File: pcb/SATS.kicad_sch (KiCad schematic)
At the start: 13 parts, among them J1 Raspberry_Pi_2_3, SW1 SW_Reed, SW2 SW_Reed, SW3 SW_Reed, U1 MCP23017_SP, U2 MCP23017_SP, U3 CD40109BE, U4 IRLZ14PBF

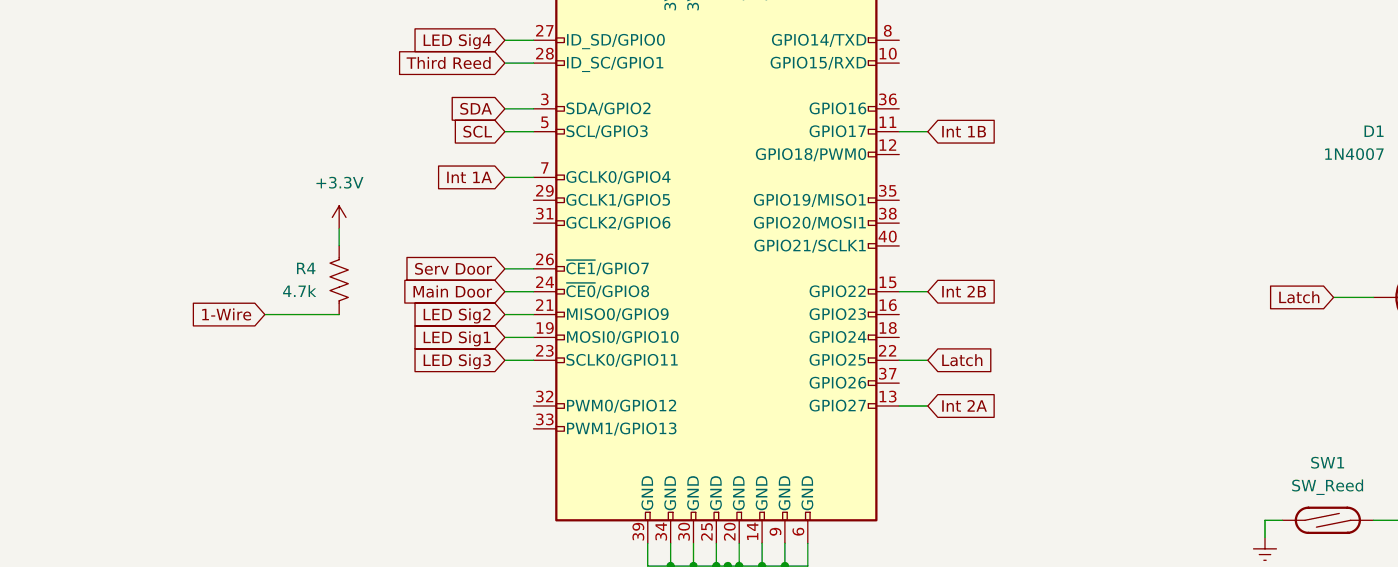
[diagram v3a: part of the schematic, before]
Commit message: actually move 1-wire
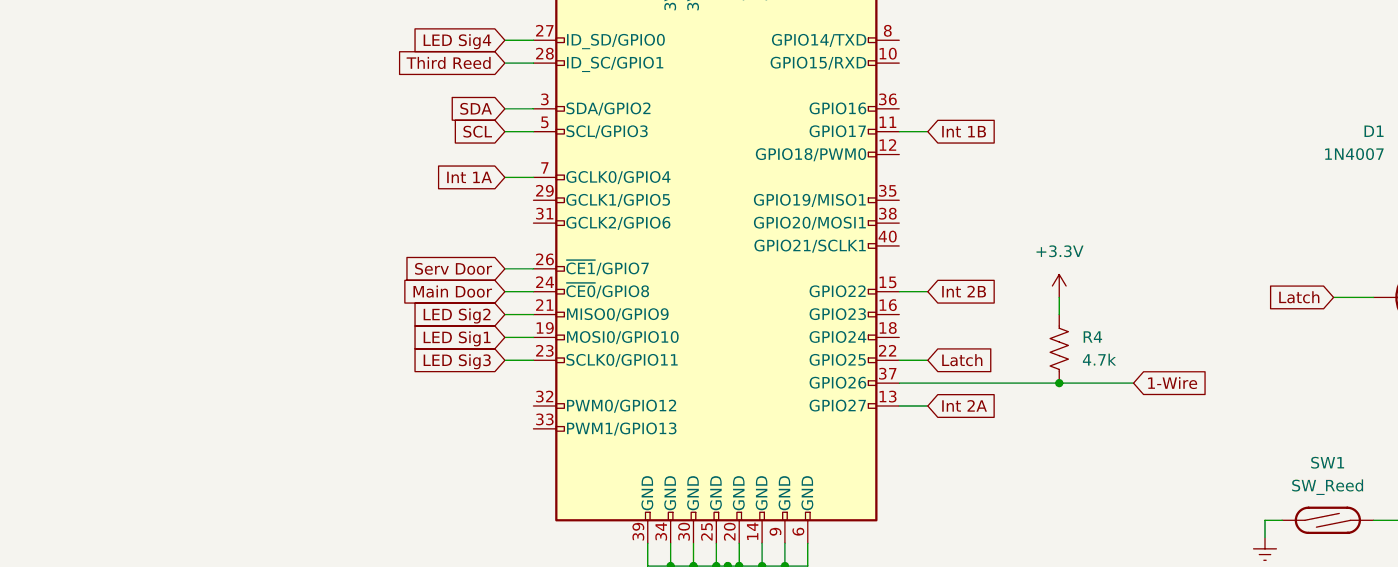
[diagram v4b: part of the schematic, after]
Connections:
- net 1-Wire: now also J1.37 (GPIO26)
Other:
- moved on the sheet: R4
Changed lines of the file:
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@@
   (junction (at 263.525 36.83) (diameter 0) (color 0 0 0 0)
   )
+  (junction (at 220.98 71.12) (diameter 0) (color 0 0 0 0)
+  )
   (junction (at 43.18 112.395) (diameter 0) (color 0 0 0 0)
   )
@@
     (stroke (width 0) (type default) (color 0 0 0 0))
   )
+  (wire (pts (xy 203.2 71.12) (xy 220.98 71.12))
+    (stroke (width 0) (type default) (color 0 0 0 0))
+  )
   (wire (pts (xy 185.42 88.9) (xy 185.42 91.44))
     (stroke (width 0) (type default) (color 0 0 0 0))
@@
     (stroke (width 0) (type default) (color 0 0 0 0))
   )
-  (wire (pts (xy 140.97 63.5) (xy 132.715 63.5))
+  (wire (pts (xy 220.98 71.12) (xy 229.235 71.12))
     (stroke (width 0) (type default) (color 0 0 0 0))
   )
@@
     (stroke (width 0) (type default) (color 0 0 0 0))
   )
-  (wire (pts (xy 140.97 53.975) (xy 140.97 55.88))
+  (wire (pts (xy 220.98 61.595) (xy 220.98 63.5))
     (stroke (width 0) (type default) (color 0 0 0 0))
   )
@@
     )
   )
-  (global_label "1-Wire" (shape input) (at 132.715 63.5 180) (fields_autoplaced)
-    (effects (font (size 1.27 1.27)) (justify right))
-    (property "Intersheet References" "${INTERSHEET_REFS}" (id 0) (at 123.589 63.4206 0)
-      (effects (font (size 1.27 1.27)) (justify right) hide)
+  (global_label "1-Wire" (shape input) (at 229.235 71.12 0) (fields_autoplaced)
+    (effects (font (size 1.27 1.27)) (justify left))
+    (property "Intersheet References" "${INTERSHEET_REFS}" (id 0) (at 238.361 71.0406 0)
+      (effects (font (size 1.27 1.27)) (justify left) hide)
     )
   )
@@
     (pin "1")
   )
-  (symbol (lib_id "power:+3.3V") (at 140.97 53.975 0) (mirror y) (unit 1)
-    (in_bom yes) (on_board yes) (fields_autoplaced)
-    (property "Reference" "#PWR?" (id 0) (at 140.97 57.785 0)
-      (effects (font (size 1.27 1.27)) hide)
-    )
-    (property "Value" "+3.3V" (id 1) (at 140.97 48.895 0))
-    (property "Footprint" "" (id 2) (at 140.97 53.975 0)
-      (effects (font (size 1.27 1.27)) hide)
-    )
-    (property "Datasheet" "" (id 3) (at 140.97 53.975 0)
+  (symbol (lib_id "power:+3.3V") (at 220.98 61.595 0) (unit 1)
+    (in_bom yes) (on_board yes) (fields_autoplaced)
+    (property "Reference" "#PWR?" (id 0) (at 220.98 65.405 0)
+      (effects (font (size 1.27 1.27)) hide)
+    )
+    (property "Value" "+3.3V" (id 1) (at 220.98 56.515 0))
+    (property "Footprint" "" (id 2) (at 220.98 61.595 0)
+      (effects (font (size 1.27 1.27)) hide)
+    )
+    (property "Datasheet" "" (id 3) (at 220.98 61.595 0)
       (effects (font (size 1.27 1.27)) hide)
     )
@@
     (pin "1")
   )
-  (symbol (lib_id "Device:R_US") (at 140.97 59.69 0) (mirror x) (unit 1)
-    (in_bom yes) (on_board yes) (fields_autoplaced)
-    (property "Reference" "R4" (id 0) (at 138.43 58.4199 0)
+  (symbol (lib_id "Device:R_US") (at 220.98 67.31 180) (unit 1)
+    (in_bom yes) (on_board yes) (fields_autoplaced)
+    (property "Reference" "R4" (id 0) (at 223.52 66.0399 0)
       (effects (font (size 1.27 1.27)) (justify right))
     )
-    (property "Value" "4.7k" (id 1) (at 138.43 60.9599 0)
+    (property "Value" "4.7k" (id 1) (at 223.52 68.5799 0)
       (effects (font (size 1.27 1.27)) (justify right))
     )
-    (property "Footprint" "" (id 2) (at 141.986 59.436 90)
-      (effects (font (size 1.27 1.27)) hide)
-    )
-    (property "Datasheet" "~" (id 3) (at 140.97 59.69 0)
-      (effects (font (size 1.27 1.27)) hide)
-    )
+    (property "Footprint" "" (id 2) (at 219.964 67.056 90)
+      (effects (font (size 1.27 1.27)) hide)
+    )
+    (property "Datasheet" "~" (id 3) (at 220.98 67.31 0)
+      (effects (font (size 1.27 1.27)) hide)
+    )

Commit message: Route jacks
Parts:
- added J2: A00-432-262-450, CONN_A00-432-262-450_EDA, symbol QuadRJ45:A00-432-262-450
- added J3: AudioJack4_SwitchTR1, symbol Connector:AudioJack4_SwitchTR1
- C1, C2: footprint (none) -> Capacitor_THT:C_Rect_L7.0mm_W3.5mm_P5.00mm
- R4: footprint (none) -> Resistor_THT:R_Axial_DIN0207_L6.3mm_D2.5mm_P7.62mm_Horizontal
- U3: footprint DIP794W45P254L1969H508Q16 -> CD40109BE:DIP794W45P254L1969H508Q16
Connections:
- net +5V: now also J2.A6, J2.B6, J2.C6, J2.D6
- net 1-Wire: now also J3.T
- net Earth: now also J2.A7, J2.B7, J2.C7, J2.D7, J3.R1, J3.R2, J3.S
- net LED3 Out: now reaches U3.11 (G)
- net LED3 Out: now also J2.C8
- net LED4 Out: now reaches U3.13 (H)
- net LED4 Out: now also J2.D8
- net LED1 Out: now reaches U3.4 (E)
- net LED1 Out: now also J2.A8
- net LED2 Out: now reaches U3.5 (F)
- net LED2 Out: now also J2.B8
- net PD_11: now reaches U1.1 (GPB0)
- net PD_11: now also J2.A1
- net PD_12: now reaches U1.2 (GPB1)
- net PD_12: now also J2.A2
- net PD_21: now reaches U1.21 (GPA0)
- net PD_21: now also J2.B1
- net PD_22: now reaches U1.22 (GPA1)
- net PD_22: now also J2.B2
- net PD_23: now reaches U1.23 (GPA2)
- net PD_23: now also J2.B3
- net PD_24: now reaches U1.24 (GPA3)
- net PD_24: now also J2.B4
- net PD_25: now reaches U1.25 (GPA4)
- net PD_25: now also J2.B5
- net PD_13: now reaches U1.3 (GPB2)
- net PD_13: now also J2.A3
- net PD_14: now reaches U1.4 (GPB3)
- net PD_14: now also J2.A4
- net PD_15: now reaches U1.5 (GPB4)
- net PD_15: now also J2.A5
- net PD_31: now reaches U2.1 (GPB0)
- net PD_31: now also J2.C1
- net PD_32: now reaches U2.2 (GPB1)
- net PD_32: now also J2.C2
- net PD_41: now reaches U2.21 (GPA0)
- net PD_41: now also J2.D1
- net PD_42: now reaches U2.22 (GPA1)
- net PD_42: now also J2.D2
- net PD_43: now reaches U2.23 (GPA2)
- net PD_43: now also J2.D3
- net PD_44: now reaches U2.24 (GPA3)
- net PD_44: now also J2.D4
- net PD_45: now reaches U2.25 (GPA4)
- net PD_45: now also J2.D5
- net PD_33: now reaches U2.3 (GPB2)
- net PD_33: now also J2.C3
- net PD_34: now reaches U2.4 (GPB3)
- net PD_34: now also J2.C4
- net PD_35: now reaches U2.5 (GPB4)
- net PD_35: now also J2.C5
- no-connect marks 0 -> 14
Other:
- moved on the sheet: C1, C2, D1, J1, L1, R4, SW1, SW2, SW3, U1, U2, U3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

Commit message: Add Alignment throughholesor jack
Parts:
- J2: footprint CONN_A00-432-262-450_EDA -> QuadRJ45:A00-432-262-450
- J3: footprint (none) -> AudioJack:AudioJack4_6pad
- U4: footprint TO220AB_VIS -> Package_TO_SOT_THT:TO-220-3_Horizontal_TabDown
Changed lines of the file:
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@@
       (effects (font (size 1.524 1.524)) (justify left))
     )
-    (property "Footprint" "CONN_A00-432-262-450_EDA" (id 2) (at 140.97 154.559 0)
+    (property "Footprint" "QuadRJ45:A00-432-262-450" (id 2) (at 140.97 154.559 0)
       (effects (font (size 1.524 1.524)) hide)
     )
@@
     (property "Reference" "J3" (id 0) (at 38.6715 105.41 0))
     (property "Value" "AudioJack4_SwitchTR1" (id 1) (at 38.6715 107.95 0))
-    (property "Footprint" "" (id 2) (at 40.64 116.84 0)
+    (property "Footprint" "AudioJack:AudioJack4_6pad" (id 2) (at 40.64 116.84 0)
       (effects (font (size 1.27 1.27)) hide)
     )
@@
       (effects (font (size 1.524 1.524)) (justify left))
     )
-    (property "Footprint" "TO220AB_VIS" (id 2) (at 205.105 152.019 0)
+    (property "Footprint" "Package_TO_SOT_THT:TO-220-3_Horizontal_TabDown" (id 2) (at 205.105 152.019 0)
       (effects (font (size 1.524 1.524)) hide)
     )
@@
     )
     (path "/06f44155-c185-4805-88c6-71de36295c8c"
-      (reference "J2") (unit 1) (value "A00-432-262-450") (footprint "CONN_A00-432-262-450_EDA")
+      (reference "J2") (unit 1) (value "A00-432-262-450") (footprint "QuadRJ45:A00-432-262-450")
     )
     (path "/7312d259-b6ec-4f2d-bfb1-01947b6a9216"
-      (reference "J3") (unit 1) (value "AudioJack4_SwitchTR1") (footprint "")
+      (reference "J3") (unit 1) (value "AudioJack4_SwitchTR1") (footprint "AudioJack:AudioJack4_6pad")
     )
     (path "/cb9438c5-536c-43dd-8dd8-607c1e8e7c09"
@@
     )
     (path "/895ab77c-6b59-440a-8f64-961029be5e6e"
-      (reference "U4") (unit 1) (value "IRLZ14PBF") (footprint "TO220AB_VIS")
-    )
-  )
+      (reference "U4") (unit 1) (value "IRLZ14PBF") (footprint "Package_TO_SOT_THT:TO-220-3_Horizontal_TabDown")
+    )
+  )

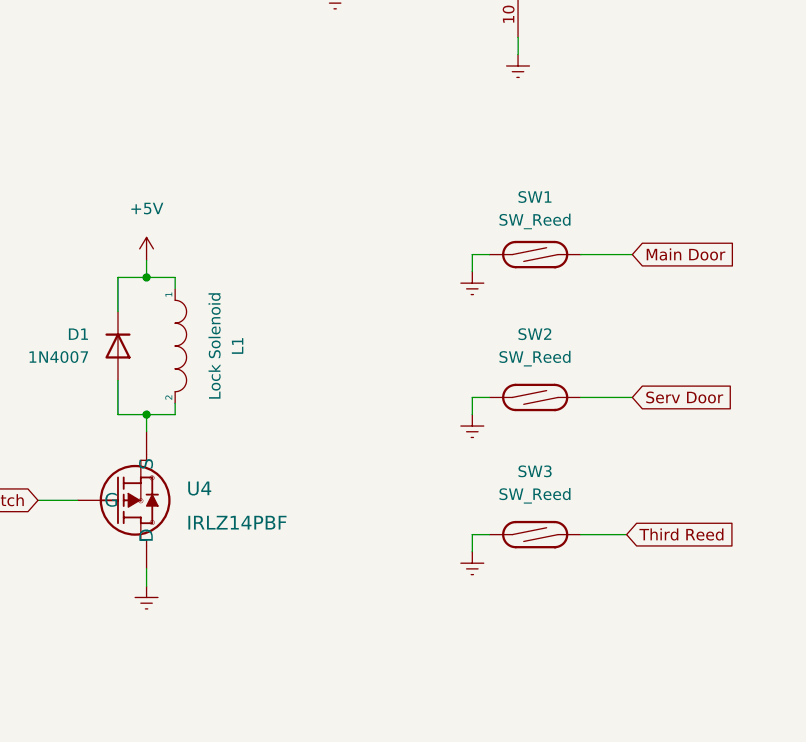
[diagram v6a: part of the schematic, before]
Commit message: Add terminal connectors for solenoid and switches
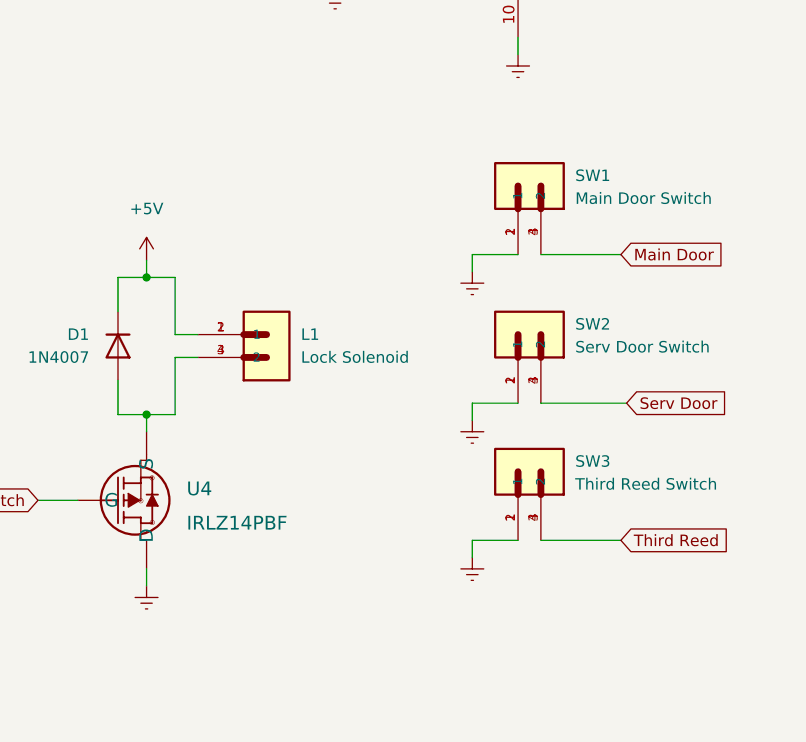
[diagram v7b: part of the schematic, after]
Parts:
- removed L1: Lock Solenoid, symbol pspice:INDUCTOR
- removed SW1, SW2, SW3: SW_Reed, symbol Switch:SW_Reed
- added L1: Lock Solenoid, TerminalConn:PHOENIX_1862042, symbol TerminalConn:1862042
- added SW1: Main Door Switch, TerminalConn:PHOENIX_1862042, symbol TerminalConn:1862042
- added SW2: Serv Door Switch, TerminalConn:PHOENIX_1862042, symbol TerminalConn:1862042
- added SW3: Third Reed Switch, TerminalConn:PHOENIX_1862042, symbol TerminalConn:1862042
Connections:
- net +5V: now also L1.1, L1.2 (1)
- net Earth: now also SW1.1, SW1.2 (1), SW2.1, SW2.2 (1), SW3.1, SW3.2 (1)
- net Main Door: now also SW1.3 (2), SW1.4 (2)
- net Serv Door: now also SW2.3 (2), SW2.4 (2)
- net Third Reed: now also SW3.3 (2), SW3.4 (2)
- net at D1.2 (A), U4.3 (S): now also L1.3 (2), L1.4 (2)
